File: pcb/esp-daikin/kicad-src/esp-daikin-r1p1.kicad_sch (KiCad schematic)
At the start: 32 parts, among them J1 PH_01x05, J2 PinHeader 1x02, U1 ESP32-C3-MINI-1, U3 AOZ1280CI

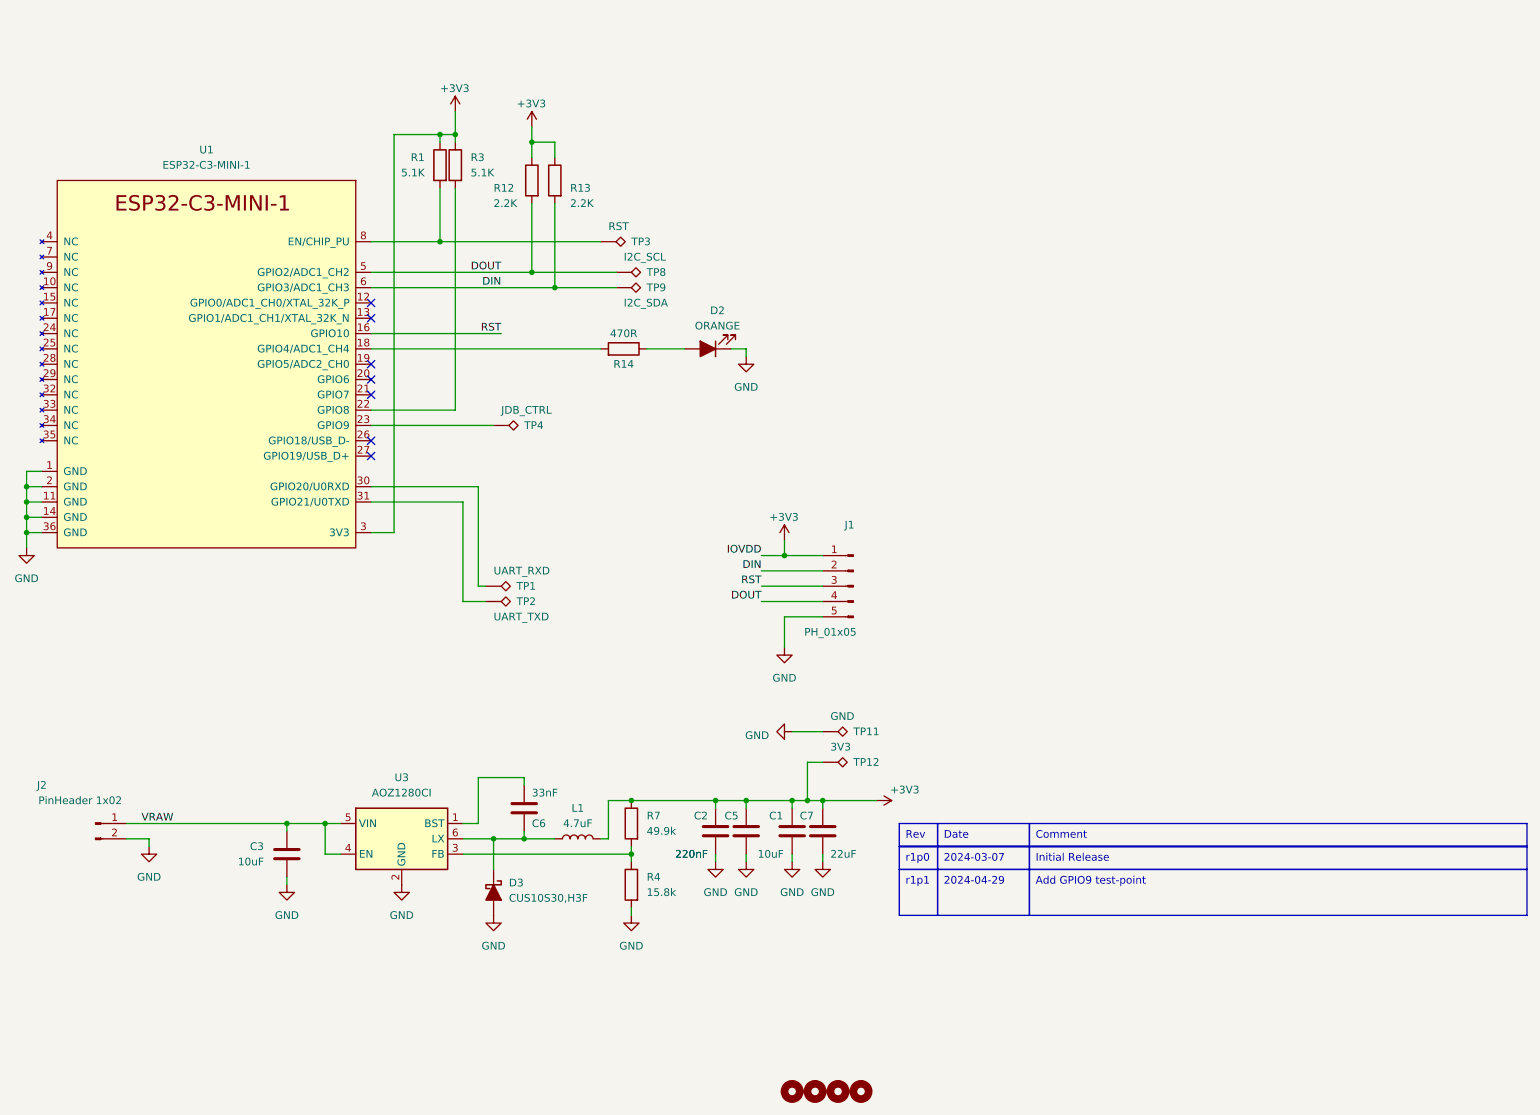
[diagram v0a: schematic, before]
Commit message: pcb.daikin-esp: Add r1p1
 - Add GPIO9 test-point to enter UART boot
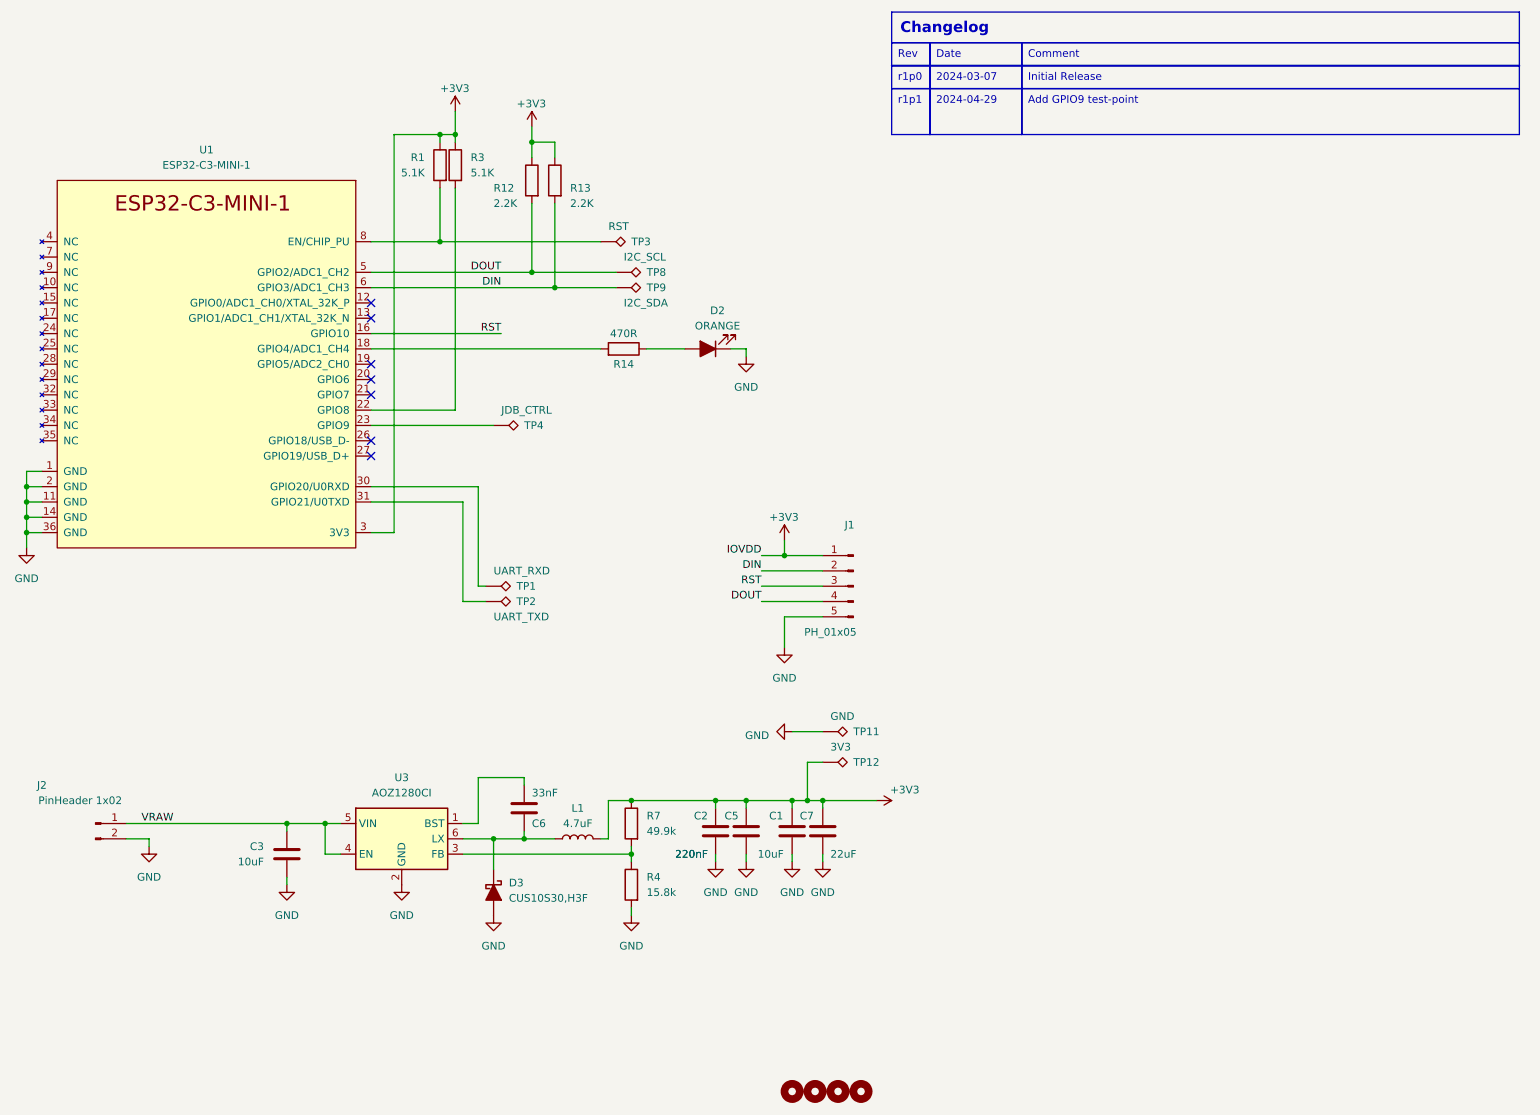
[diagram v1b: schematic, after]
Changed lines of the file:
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@@
 	(polyline
 		(pts
-			(xy 179.07 152.4) (xy 283.21 152.4)
+			(xy 177.8 22.86) (xy 281.94 22.86)
 		)
 		(stroke
@@
 	)
 	(image
-		(at 224.79 49.53)
-		(scale 2.09558)
+		(at 248.92 60.96)
+		(scale 1.61617)
 		(data "iVBORw0KGgoAAAANSUhEUgAAAcAAAAEmCAYAAAD1OEDsAAAABHNCSVQICAgIfAhkiAAAABl0RVh0"
 			"U29mdHdhcmUAZ25vbWUtc2NyZWVuc2hvdO8Dvz4AAAAmdEVYdENyZWF0aW9uIFRpbWUATW9uIDI5"
@@
 	(text_box "Add GPIO9 test-point"
 		(exclude_from_sim no)
-		(at 200.66 156.21 0)
+		(at 199.39 26.67 0)
 		(size 82.55 7.62)
 		(stroke
@@
 	(text_box "Date"
 		(exclude_from_sim no)
-		(at 185.42 148.59 0)
+		(at 184.15 19.05 0)
 		(size 15.24 3.81)
 		(stroke
@@
 	(text_box "r1p0"
 		(exclude_from_sim no)
-		(at 179.07 152.4 0)
+		(at 177.8 22.86 0)
 		(size 6.35 3.81)
 		(stroke
@@
 		)
 	)
+	(text_box "Changelog"
+		(exclude_from_sim no)
+		(at 177.8 13.97 0)
+		(size 104.14 5.08)
+		(stroke
+			(width 0)
+			(type default)
+		)
+		(fill
+			(type none)
+		)
+		(effects
+			(font
+				(size 1.8 1.8)
+				(thickness 0.36)
+				(bold yes)
+			)
+			(justify left top)
+		)
+	)
 	(text_box "Rev"
 		(exclude_from_sim no)
-		(at 179.07 148.59 0)
+		(at 177.8 19.05 0)
 		(size 6.35 3.81)
 		(stroke
@@
 	(text_box "Comment"
 		(exclude_from_sim no)
-		(at 200.66 148.59 0)
+		(at 199.39 19.05 0)
 		(size 82.55 3.81)
 		(stroke
@@
 	(text_box "2024-03-07"
 		(exclude_from_sim no)
-		(at 185.42 152.4 0)
+		(at 184.15 22.86 0)
 		(size 15.24 3.81)
 		(stroke
@@
 	(text_box "2024-04-29"
 		(exclude_from_sim no)
-		(at 185.42 156.21 0)
+		(at 184.15 26.67 0)
 		(size 15.24 7.62)
 		(stroke
@@
 	(text_box "Initial Release"
 		(exclude_from_sim no)
-		(at 200.66 152.4 0)
+		(at 199.39 22.86 0)
 		(size 82.55 3.81)
 		(stroke
@@
 	(text_box "r1p1"
 		(exclude_from_sim no)
-		(at 179.07 156.21 0)
+		(at 177.8 26.67 0)
 		(size 6.35 7.62)
 		(stroke
@@
 		)
 		(instances
-			(project "esp-daikin-r1p0"
+			(project "esp-daikin-r1p1"
 				(path "/81d8eb84-5504-4697-9960-5d51224de127"
 					(reference "#PWR0102")
@@
 		)
 		(instances
-			(project "esp-daikin-r1p0"
+			(project "esp-daikin-r1p1"
 				(path "/81d8eb84-5504-4697-9960-5d51224de127"
 					(reference "U1")
@@
 		)
 		(instances
-			(project "esp-daikin-r1p0"
+			(project "esp-daikin-r1p1"
 				(path "/81d8eb84-5504-4697-9960-5d51224de127"
 					(reference "TP4")
@@
 		)
 		(instances
-			(project "esp-daikin-r1p0"
+			(project "esp-daikin-r1p1"
 				(path "/81d8eb84-5504-4697-9960-5d51224de127"
 					(reference "C1")
@@
 		)
 		(instances
-			(project "esp-daikin-r1p0"
+			(project "esp-daikin-r1p1"
 				(path "/81d8eb84-5504-4697-9960-5d51224de127"
 					(reference "C3")
@@
 		)
 		(instances
-			(project "esp-daikin-r1p0"
+			(project "esp-daikin-r1p1"
 				(path "/81d8eb84-5504-4697-9960-5d51224de127"
 					(reference "C6")
@@
 		)
 		(instances
-			(project "esp-daikin-r1p0"
+			(project "esp-daikin-r1p1"
 				(path "/81d8eb84-5504-4697-9960-5d51224de127"
 					(reference "H2")
@@
 		)
 		(instances
-			(project "esp-daikin-r1p0"
+			(project "esp-daikin-r1p1"
 				(path "/81d8eb84-5504-4697-9960-5d51224de127"
 					(reference "TP8")
@@
 		)
 		(instances
-			(project "esp-daikin-r1p0"
+			(project "esp-daikin-r1p1"
 				(path "/81d8eb84-5504-4697-9960-5d51224de127"
 					(reference "H3")
@@
 		)
 		(instances
-			(project "esp-daikin-r1p0"
+			(project "esp-daikin-r1p1"
 				(path "/81d8eb84-5504-4697-9960-5d51224de127"
 					(reference "#PWR010")
@@
 		)
 		(instances
-			(project "esp-daikin-r1p0"
+			(project "esp-daikin-r1p1"
 				(path "/81d8eb84-5504-4697-9960-5d51224de127"
 					(reference "J2")
@@
 		)
 		(instances
-			(project "esp-daikin-r1p0"
+			(project "esp-daikin-r1p1"
 				(path "/81d8eb84-5504-4697-9960-5d51224de127"
 					(reference "#PWR03")
@@
 		)
 		(instances
-			(project "esp-daikin-r1p0"
+			(project "esp-daikin-r1p1"
 				(path "/81d8eb84-5504-4697-9960-5d51224de127"
 					(reference "R3")
@@
 		)
 		(instances
-			(project "esp-daikin-r1p0"
+			(project "esp-daikin-r1p1"
 				(path "/81d8eb84-5504-4697-9960-5d51224de127"
 					(reference "#PWR06")
@@
 		)
 		(instances
-			(project "esp-daikin-r1p0"
+			(project "esp-daikin-r1p1"
 				(path "/81d8eb84-5504-4697-9960-5d51224de127"
 					(reference "#PWR04")
@@
 		)
 		(instances
-			(project "esp-daikin-r1p0"
+			(project "esp-daikin-r1p1"
 				(path "/81d8eb84-5504-4697-9960-5d51224de127"
 					(reference "#PWR08")
@@
 		)
 		(instances
-			(project "esp-daikin-r1p0"
+			(project "esp-daikin-r1p1"
 				(path "/81d8eb84-5504-4697-9960-5d51224de127"
 					(reference "D2")
@@
 		)
 		(instances
-			(project "esp-daikin-r1p0"
+			(project "esp-daikin-r1p1"
 				(path "/81d8eb84-5504-4697-9960-5d51224de127"
 					(reference "#PWR07")
@@
 		)
 		(instances
-			(project "esp-daikin-r1p0"
+			(project "esp-daikin-r1p1"
 				(path "/81d8eb84-5504-4697-9960-5d51224de127"
 					(reference "R12")
@@
 		)
 		(instances
-			(project "esp-daikin-r1p0"
+			(project "esp-daikin-r1p1"
 				(path "/81d8eb84-5504-4697-9960-5d51224de127"
 					(reference "#PWR01")
@@
 		)
 		(instances
-			(project "esp-daikin-r1p0"
+			(project "esp-daikin-r1p1"
 				(path "/81d8eb84-5504-4697-9960-5d51224de127"
 					(reference "D3")
@@
 		)
 		(instances
-			(project "esp-daikin-r1p0"
+			(project "esp-daikin-r1p1"
 				(path "/81d8eb84-5504-4697-9960-5d51224de127"
 					(reference "TP1")
@@
 		)
 		(instances
-			(project "esp-daikin-r1p0"
+			(project "esp-daikin-r1p1"
 				(path "/81d8eb84-5504-4697-9960-5d51224de127"
 					(reference "L1")
@@
 		)
 		(instances
-			(project "esp-daikin-r1p0"
+			(project "esp-daikin-r1p1"
 				(path "/81d8eb84-5504-4697-9960-5d51224de127"
 					(reference "#PWR02")
@@
 		)
 		(instances
-			(project "esp-daikin-r1p0"
+			(project "esp-daikin-r1p1"
 				(path "/81d8eb84-5504-4697-9960-5d51224de127"
 					(reference "J1")
@@
 		)
 		(instances
-			(project "esp-daikin-r1p0"
+			(project "esp-daikin-r1p1"
 				(path "/81d8eb84-5504-4697-9960-5d51224de127"
 					(reference "C5")
@@
 		)
 		(instances
-			(project "esp-daikin-r1p0"
+			(project "esp-daikin-r1p1"
 				(path "/81d8eb84-5504-4697-9960-5d51224de127"
 					(reference "R13")
@@
 		)
 		(instances
-			(project "esp-daikin-r1p0"
+			(project "esp-daikin-r1p1"
 				(path "/81d8eb84-5504-4697-9960-5d51224de127"
 					(reference "#PWR0101")
@@
 		)
 		(instances
-			(project "esp-daikin-r1p0"
+			(project "esp-daikin-r1p1"
 				(path "/81d8eb84-5504-4697-9960-5d51224de127"
 					(reference "H1")
@@
 		)
 		(instances
-			(project "esp-daikin-r1p0"
+			(project "esp-daikin-r1p1"
 				(path "/81d8eb84-5504-4697-9960-5d51224de127"
 					(reference "#PWR0124")
@@
 		)
 		(instances
-			(project "esp-daikin-r1p0"
+			(project "esp-daikin-r1p1"
 				(path "/81d8eb84-5504-4697-9960-5d51224de127"
 					(reference "R4")
@@
 		)
 		(instances
-			(project "esp-daikin-r1p0"
+			(project "esp-daikin-r1p1"
 				(path "/81d8eb84-5504-4697-9960-5d51224de127"
 					(reference "TP2")
@@
 		)
 		(instances
-			(project "esp-daikin-r1p0"
+			(project "esp-daikin-r1p1"
 				(path "/81d8eb84-5504-4697-9960-5d51224de127"
 					(reference "U3")
@@
 		)
 		(instances
-			(project "esp-daikin-r1p0"
+			(project "esp-daikin-r1p1"
 				(path "/81d8eb84-5504-4697-9960-5d51224de127"
 					(reference "TP3")
@@
 		)
 		(instances
-			(project "esp-daikin-r1p0"
+			(project "esp-daikin-r1p1"
 				(path "/81d8eb84-5504-4697-9960-5d51224de127"
 					(reference "#PWR0122")
@@
 		)
 		(instances
-			(project "esp-daikin-r1p0"
+			(project "esp-daikin-r1p1"
 				(path "/81d8eb84-5504-4697-9960-5d51224de127"
 					(reference "R7")
@@
 		)
 		(instances
-			(project "esp-daikin-r1p0"
+			(project "esp-daikin-r1p1"
 				(path "/81d8eb84-5504-4697-9960-5d51224de127"
 					(reference "#PWR0123")
@@
 		)
 		(instances
-			(project "esp-daikin-r1p0"
+			(project "esp-daikin-r1p1"
 				(path "/81d8eb84-5504-4697-9960-5d51224de127"
 					(reference "TP11")
@@
 		)
 		(instances
-			(project "esp-daikin-r1p0"
+			(project "esp-daikin-r1p1"
 				(path "/81d8eb84-5504-4697-9960-5d51224de127"
 					(reference "#PWR0103")
@@
 		)
 		(instances
-			(project "esp-daikin-r1p0"
+			(project "esp-daikin-r1p1"
 				(path "/81d8eb84-5504-4697-9960-5d51224de127"
 					(reference "TP9")
@@
 		)
 		(instances
-			(project "esp-daikin-r1p0"
+			(project "esp-daikin-r1p1"
 				(path "/81d8eb84-5504-4697-9960-5d51224de127"
 					(reference "C2")
@@
 		)
 		(instances
-			(project "esp-daikin-r1p0"
+			(project "esp-daikin-r1p1"
 				(path "/81d8eb84-5504-4697-9960-5d51224de127"
 					(reference "R1")
@@
 		)
 		(instances
-			(project "esp-daikin-r1p0"
+			(project "esp-daikin-r1p1"
 				(path "/81d8eb84-5504-4697-9960-5d51224de127"
 					(reference "C7")
@@
 		)
 		(instances
-			(project "esp-daikin-r1p0"
+			(project "esp-daikin-r1p1"
 				(path "/81d8eb84-5504-4697-9960-5d51224de127"
 					(reference "TP12")
@@
 		)
 		(instances
-			(project "esp-daikin-r1p0"
+			(project "esp-daikin-r1p1"
 				(path "/81d8eb84-5504-4697-9960-5d51224de127"
 					(reference "#PWR05")
@@
 		)
 		(instances
-			(project "esp-daikin-r1p0"
+			(project "esp-daikin-r1p1"
 				(path "/81d8eb84-5504-4697-9960-5d51224de127"
 					(reference "#PWR09")
@@
 		)
 		(instances
-			(project "esp-daikin-r1p0"
+			(project "esp-daikin-r1p1"
 				(path "/81d8eb84-5504-4697-9960-5d51224de127"
 					(reference "R14")
@@
 		)
 		(instances
-			(project "esp-daikin-r1p0"
+			(project "esp-daikin-r1p1"
 				(path "/81d8eb84-5504-4697-9960-5d51224de127"
 					(reference "H4")
@@
 		)
 		(instances
-			(project "esp-daikin-r1p0"
+			(project "esp-daikin-r1p1"
 				(path "/81d8eb84-5504-4697-9960-5d51224de127"
 					(reference "#PWR011")

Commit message: fix(pcb): fix C3 part number
fixes #3
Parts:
- C1: LCSC C19702 -> C96446
- C3: LCSC C15850 -> C96446
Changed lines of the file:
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@@
 			)
 		)
-		(property "LCSC" "C19702"
+		(property "LCSC" "C96446"
 			(at 157.48 147.32 0)
 			(effects
@@
 			)
 		)
-		(property "LCSC" "C15850"
+		(property "LCSC" "C96446"
 			(at 73.66 152.4 0)
 			(effects
